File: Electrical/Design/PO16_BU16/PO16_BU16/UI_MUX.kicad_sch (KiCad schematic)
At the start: 18 parts, among them U701 74HC4051

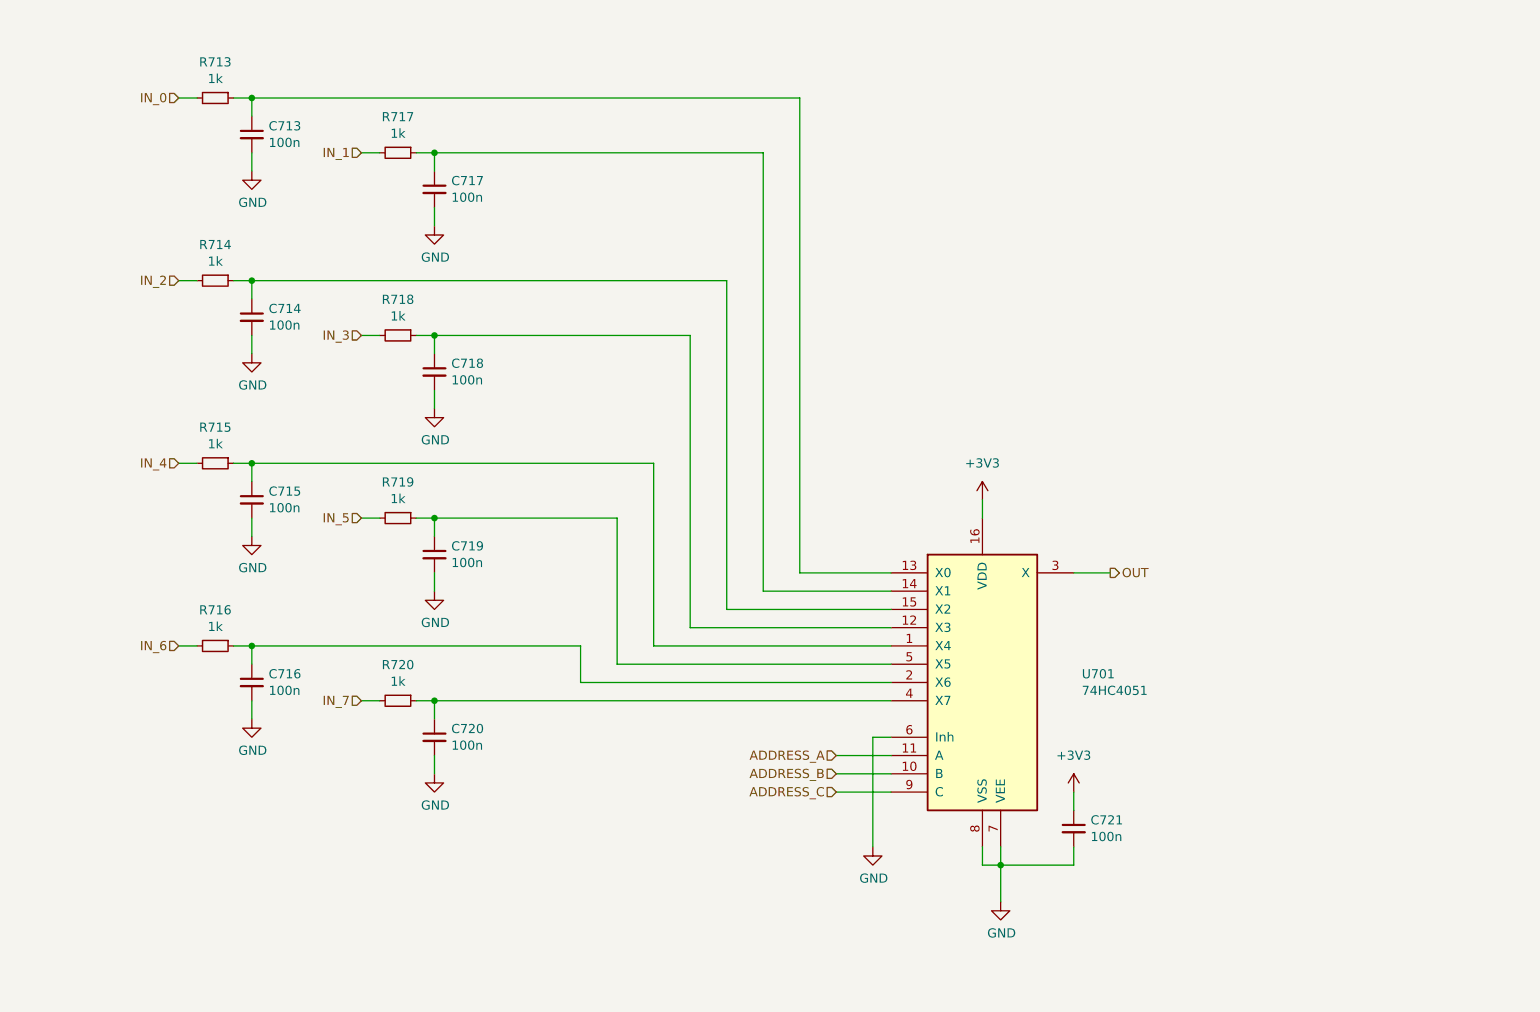
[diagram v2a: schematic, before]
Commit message: SUKU PO16_BU16 sch reannotated
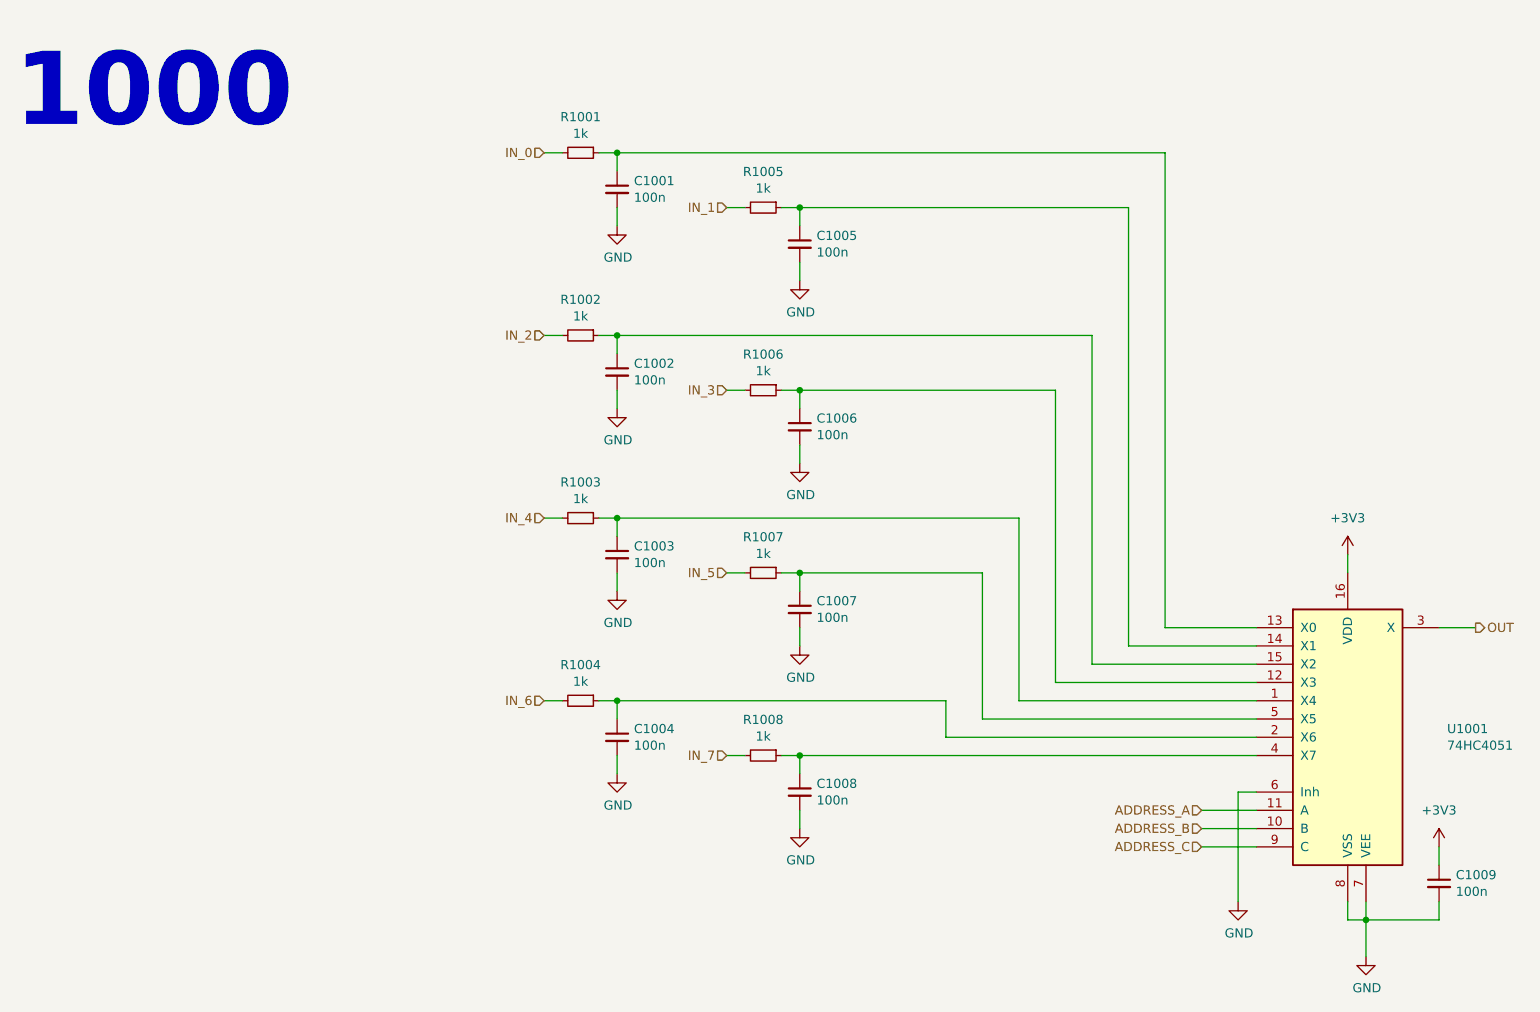
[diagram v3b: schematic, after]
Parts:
- renumbered C713 to C1001, C714 to C1002, C715 to C1003, C716 to C1004, C717 to C1005, C718 to C1006, C719 to C1007, C720 to C1008, C721 to C1009, R713 to R1001, R714 to R1002, R715 to R1003, R716 to R1004, R717 to R1005, R718 to R1006, R719 to R1007, R720 to R1008, U701 to U1001
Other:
- note added: "1000"
- moved on the sheet: C1001, C1002, C1003, C1004, C1005, C1006, C1007, C1008, C1009, R1001, R1002, R1003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
